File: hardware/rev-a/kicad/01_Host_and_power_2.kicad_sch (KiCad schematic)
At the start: 5 parts

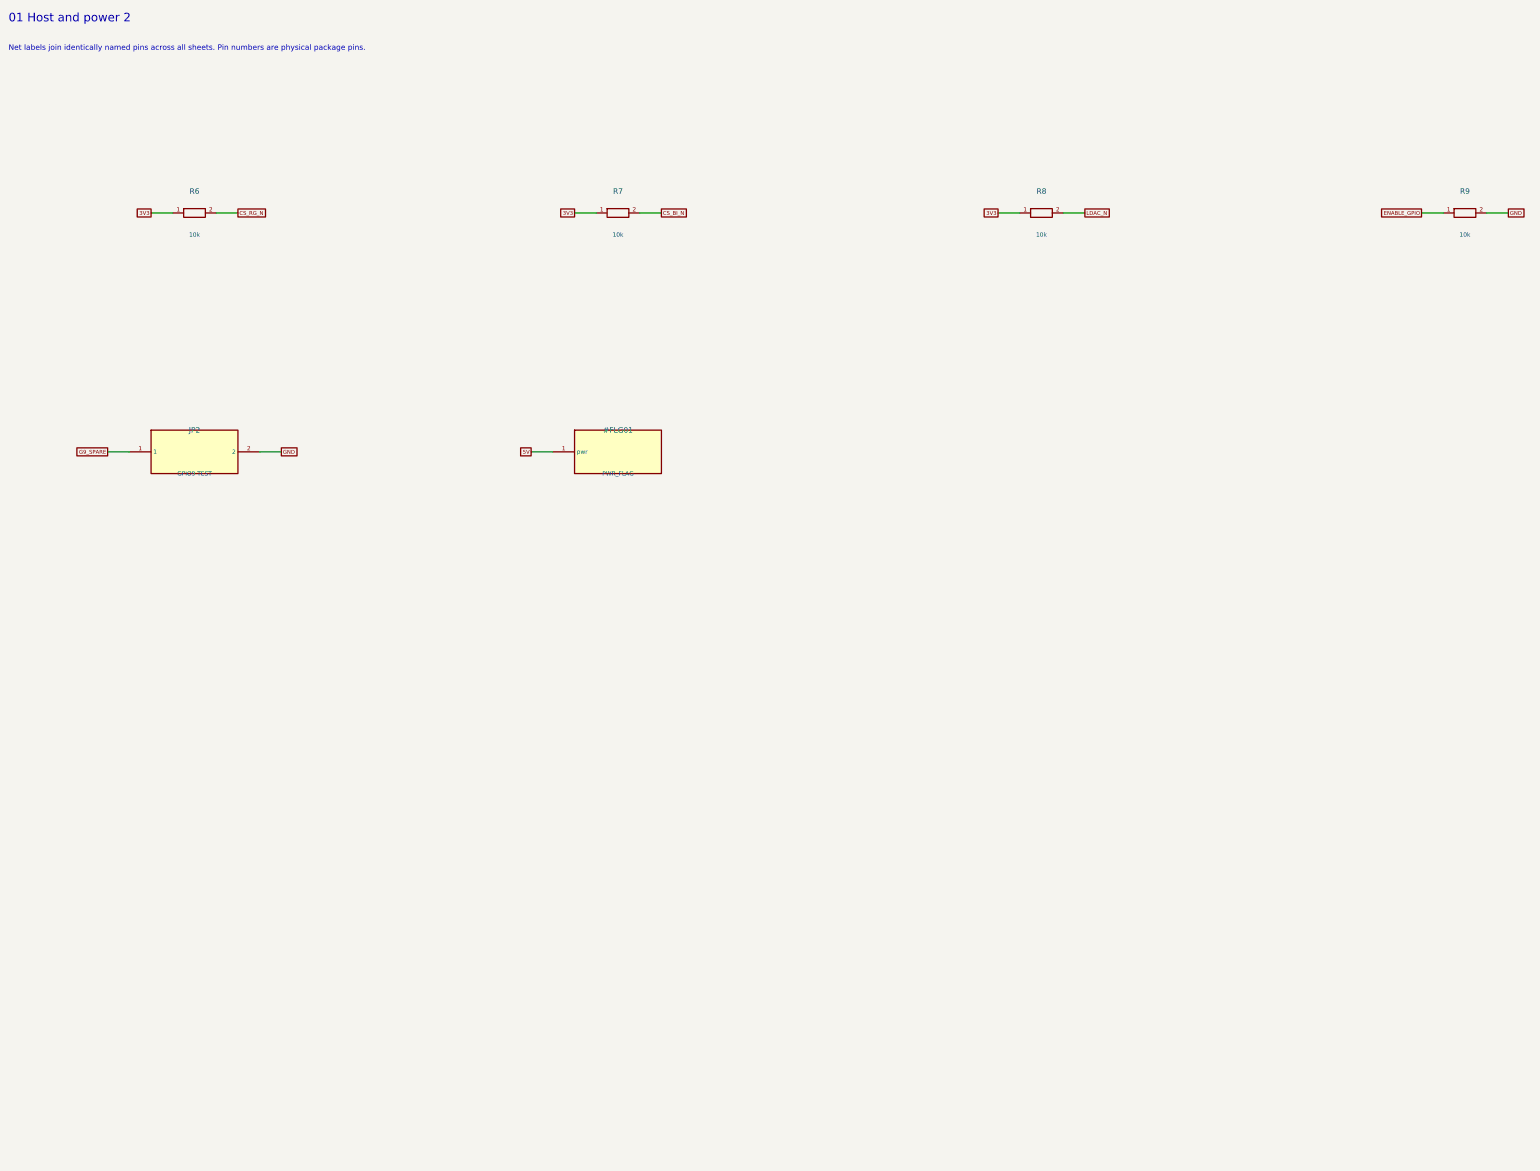
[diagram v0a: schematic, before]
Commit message: Redraw Rev.A schematics with functional blocks and explicit wiring
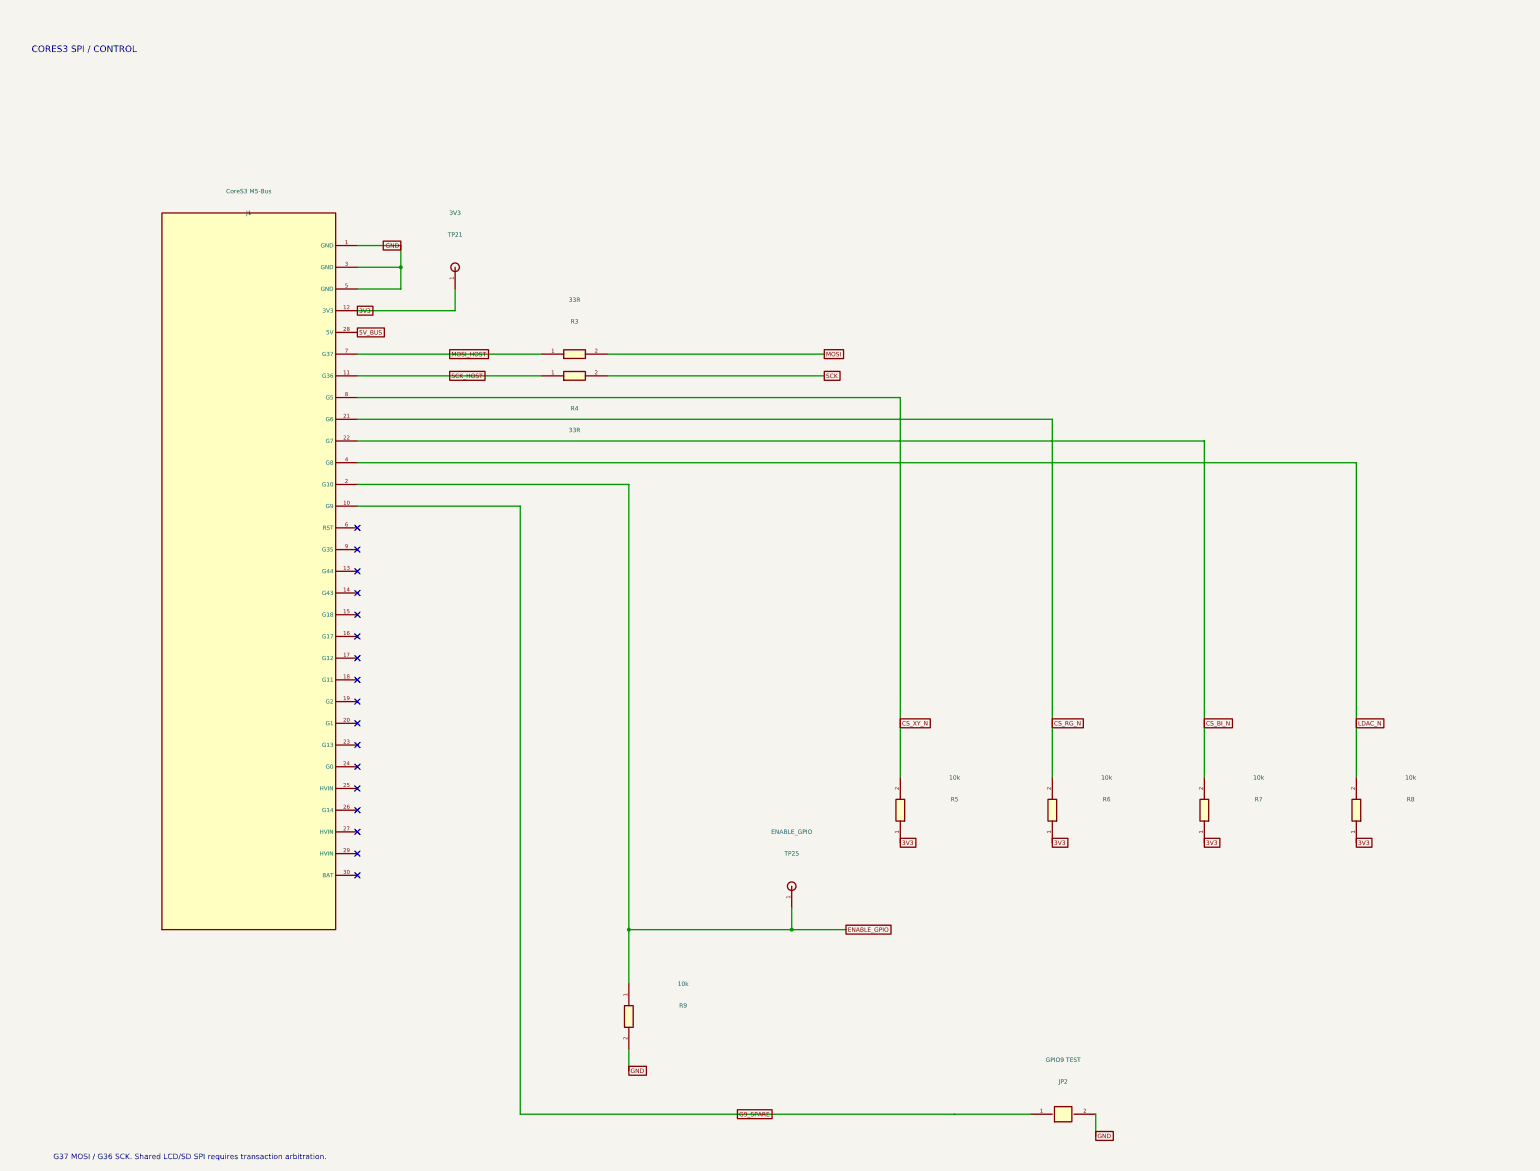
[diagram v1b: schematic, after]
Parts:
- added J1: CoreS3 M5-Bus, RevA:M5Bus_CoreS3_TypeA, symbol RevA:Part_J1
- added R3, R4: 33R, RevA:R_Axial_DIN0207_L6.3mm_D2.5mm_P10.16mm_Horizontal, symbol RevA:R
- added R5: 10k, RevA:R_Axial_DIN0207_L6.3mm_D2.5mm_P10.16mm_Horizontal, symbol RevA:R
- added TP21: 3V3, RevA:TestPoint_THTPad_D2.0mm_Drill1.0mm, symbol RevA:TP
- added TP25: ENABLE_GPIO, RevA:TestPoint_THTPad_D2.0mm_Drill1.0mm, symbol RevA:TP
- JP2: symbol RevA:Conn_JP2 -> RevA:Link
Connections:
- net 3V3: now also J1.12 (3V3), R5.1, TP21.1
- net CS_BI_N: now also J1.22 (G7)
- net CS_RG_N: now also J1.21 (G6)
- net ENABLE_GPIO: now also J1.2 (G10), TP25.1
- net G9_SPARE: now also J1.10 (G9)
- net GND: now also J1.1 (GND), J1.3 (GND), J1.5 (GND)
- net LDAC_N: now also J1.4 (G8)
- new net 5V_BUS: J1.28 (5V)
- new net CS_XY_N: J1.8 (G5), R5.2
- new net MOSI: R3.2
- new net MOSI_HOST: J1.7 (G37), R3.1
- new net SCK: R4.2
- new net SCK_HOST: J1.11 (G36), R4.1
- no-connect marks 0 -> 17
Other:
- note added: "CORES3 SPI / CONTROL"
- note added: "G37 MOSI / G36 SCK. Shared LCD/SD SPI requires transaction arbitration."
- note removed: "01 Host and power 2"
- note removed: "Net labels join identically named pins across all sheets. Pin numbers are physical package pins."
- company: CoreS3 ILDA evaluation -> (none)
- title: 01_Host_and_power_2 -> 02 / CoreS3 bus and digital control
